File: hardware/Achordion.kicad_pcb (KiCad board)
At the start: 2 copper layers, 44.5 x 109.4 mm, 100 parts, among them J1 Power, J10 Jack, J11 Jack, J4 Jack, J5 Jack, J6 Jack, J7 Jack, J8 Jack, J9 Jack, SW2 Button, U4 LM4040C10, U6 TL072, U7 MCP6002, U8 MCP6002, U9 MCP6002

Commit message: Release version 0.10.0
Signed-off-by: Petr Horacek <hrck@protonmail.com>
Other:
- board text added: "board v0.10.0"
- board text removed: "board v0.9.0"

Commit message: Release version 0.11.0
Signed-off-by: Petr Horacek <hrck@protonmail.com>
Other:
- board text added: "board v0.11.0"
- board text removed: "board v0.10.0"
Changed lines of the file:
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@@
     (title Achordion)
     (date 2021-04-25)
-    (rev v0.10.0)
+    (rev v0.11.0)
     (company "Petr Horáček")
     (comment 1 hrck@protonmail.com)
@@
   (gr_circle (center 162.726001 144.48) (end 164.237002 144.48) (layer Edge.Cuts) (width 0.1))
   (gr_circle (center 139.236001 129.55) (end 140.747002 129.55) (layer Edge.Cuts) (width 0.1))
-  (gr_text "board v0.10.0" (at 156.325 42.775) (layer F.SilkS)
+  (gr_text "board v0.11.0" (at 156.325 42.775) (layer F.SilkS)
     (effects (font (size 1 1) (thickness 0.15)) (justify left))
   )

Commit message: Release version 0.12.0
Signed-off-by: Petr Horacek <hrck@protonmail.com>
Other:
- board text added: "board v0.12.0"
- board text removed: "board v0.11.0"
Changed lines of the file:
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@@
     (title Achordion)
     (date 2021-04-25)
-    (rev v0.11.0)
+    (rev v0.12.0)
     (company "Petr Horáček")
     (comment 1 hrck@protonmail.com)
@@
   (gr_circle (center 162.726001 144.48) (end 164.237002 144.48) (layer Edge.Cuts) (width 0.1))
   (gr_circle (center 139.236001 129.55) (end 140.747002 129.55) (layer Edge.Cuts) (width 0.1))
-  (gr_text "board v0.11.0" (at 156.325 42.775) (layer F.SilkS)
+  (gr_text "board v0.12.0" (at 156.325 42.775) (layer F.SilkS)
     (effects (font (size 1 1) (thickness 0.15)) (justify left))
   )

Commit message: Release version 0.13.0
Signed-off-by: Petr Horacek <hrck@protonmail.com>
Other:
- board text added: "board v0.13.0"
- board text removed: "board v0.12.0"
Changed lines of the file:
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@@
     (title Achordion)
     (date 2021-04-25)
-    (rev v0.12.0)
+    (rev v0.13.0)
     (company "Petr Horáček")
     (comment 1 hrck@protonmail.com)
@@
   (gr_circle (center 162.726001 144.48) (end 164.237002 144.48) (layer Edge.Cuts) (width 0.1))
   (gr_circle (center 139.236001 129.55) (end 140.747002 129.55) (layer Edge.Cuts) (width 0.1))
-  (gr_text "board v0.12.0" (at 156.325 42.775) (layer F.SilkS)
+  (gr_text "board v0.13.0" (at 156.325 42.775) (layer F.SilkS)
     (effects (font (size 1 1) (thickness 0.15)) (justify left))
   )

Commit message: Release version 0.14.0
Signed-off-by: Petr Horacek <hrck@protonmail.com>
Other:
- board text added: "board v0.14.0"
- board text removed: "board v0.13.0"
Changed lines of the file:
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@@
     (title Achordion)
     (date 2021-04-25)
-    (rev v0.13.0)
+    (rev v0.14.0)
     (company "Petr Horáček")
     (comment 1 hrck@protonmail.com)
@@
   (gr_circle (center 162.726001 144.48) (end 164.237002 144.48) (layer Edge.Cuts) (width 0.1))
   (gr_circle (center 139.236001 129.55) (end 140.747002 129.55) (layer Edge.Cuts) (width 0.1))
-  (gr_text "board v0.13.0" (at 156.325 42.775) (layer F.SilkS)
+  (gr_text "board v0.14.0" (at 156.325 42.775) (layer F.SilkS)
     (effects (font (size 1 1) (thickness 0.15)) (justify left))
   )

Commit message: Release version 0.15.0
Signed-off-by: Petr Horacek <hrck@protonmail.com>
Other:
- board text added: "board v0.15.0"
- board text removed: "board v0.14.0"
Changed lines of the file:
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@@
     (title Achordion)
     (date 2021-04-25)
-    (rev v0.14.0)
+    (rev v0.15.0)
     (company "Petr Horáček")
     (comment 1 hrck@protonmail.com)
@@
   (gr_circle (center 162.726001 144.48) (end 164.237002 144.48) (layer Edge.Cuts) (width 0.1))
   (gr_circle (center 139.236001 129.55) (end 140.747002 129.55) (layer Edge.Cuts) (width 0.1))
-  (gr_text "board v0.14.0" (at 156.325 42.775) (layer F.SilkS)
+  (gr_text "board v0.15.0" (at 156.325 42.775) (layer F.SilkS)
     (effects (font (size 1 1) (thickness 0.15)) (justify left))
   )

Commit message: Release version 0.16.0
Signed-off-by: Petr Horacek <hrck@protonmail.com>
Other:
- board text added: "board v0.16.0"
- board text removed: "board v0.15.0"
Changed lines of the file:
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@@
     (title Achordion)
     (date 2021-04-25)
-    (rev v0.15.0)
+    (rev v0.16.0)
     (company "Petr Horáček")
     (comment 1 hrck@protonmail.com)
@@
   (gr_circle (center 162.726001 144.48) (end 164.237002 144.48) (layer Edge.Cuts) (width 0.1))
   (gr_circle (center 139.236001 129.55) (end 140.747002 129.55) (layer Edge.Cuts) (width 0.1))
-  (gr_text "board v0.15.0" (at 156.325 42.775) (layer F.SilkS)
+  (gr_text "board v0.16.0" (at 156.325 42.775) (layer F.SilkS)
     (effects (font (size 1 1) (thickness 0.15)) (justify left))
   )

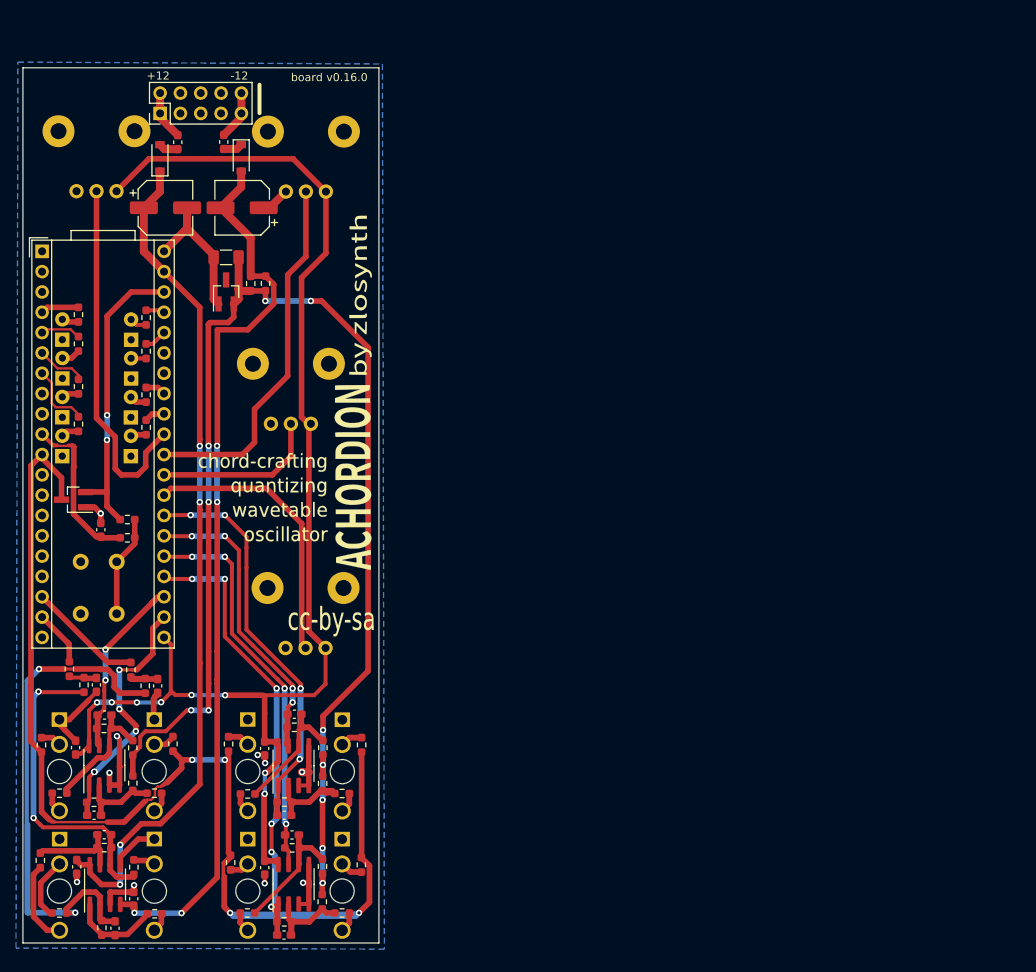
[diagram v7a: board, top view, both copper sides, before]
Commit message: Convert PCB to two stacked layers
This completely reworked layout should be much easier to solder and also
follows new front panel layout.

Signed-off-by: Petr Horacek <hrck@protonmail.com>
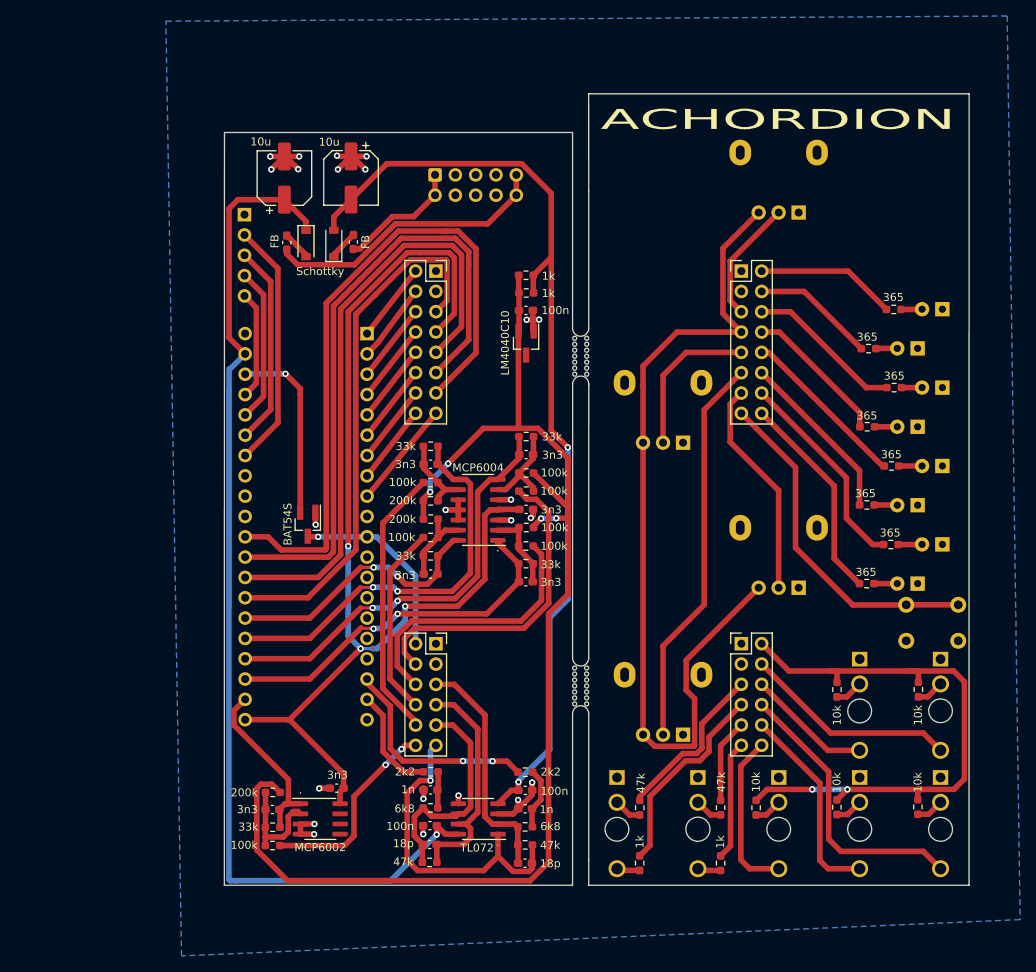
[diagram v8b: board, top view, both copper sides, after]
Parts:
- removed C39: 100n, Capacitor_SMD:C_0603_1608Metric_Pad1.08x0.95mm_HandSolder
- removed C45, C47: 3n3, Capacitor_SMD:C_0603_1608Metric_Pad1.08x0.95mm_HandSolder
- removed G***: LOGO, Graphics:Graphics_Back
- removed G***: LOGO, Graphics:Graphics_Front
- removed R15, R16, R49: 10k, Resistor_SMD:R_0603_1608Metric_Pad0.98x0.95mm_HandSolder
- removed R32: 200k, Resistor_SMD:R_0603_1608Metric_Pad0.98x0.95mm_HandSolder
- removed R33: 100k, Resistor_SMD:R_0603_1608Metric_Pad0.98x0.95mm_HandSolder
- removed R34: 33k, Resistor_SMD:R_0603_1608Metric_Pad0.98x0.95mm_HandSolder
- removed U7, U8: MCP6002, Package_SO:SOIC-8_3.9x4.9mm_P1.27mm
- added J12: Debug, Connector_PinHeader_2.54mm:PinHeader_1x05_P2.54mm_Vertical, B.Cu at (150.5, 59.9)
- added J13: A IFACE, Connector_PinHeader_2.54mm:PinHeader_2x08_P2.54mm_Vertical, F.Cu at (212.6, 67.0)
- added J2: B IFACE, Connector_PinSocket_2.54mm:PinSocket_2x08_P2.54mm_Vertical, F.Cu at (174.4, 67.0)
- added J3: B I/O, Connector_PinSocket_2.54mm:PinSocket_2x06_P2.54mm_Vertical, F.Cu at (174.4, 113.6)
- added U1: MCP6004, Package_SO:SOIC-14_3.9x8.7mm_P1.27mm, F.Cu at (179.7, 96.8)
- added mouse-bite-2mm-slot: VAL**, Panelization:mouse-bite-2mm-slot, F.Cu at (192.6, 118.8)
- added mouse-bite-2mm-slot: VAL**, Panelization:mouse-bite-2mm-slot, F.Cu at (192.6, 77.6)
- A1: value DaisySeed_Rev4 -> Daisy Seed v4; footprint Socket_DaisySeed:DaisySeed -> Device_Audio_Electrosmith_Daisy_Seed:Device_Audio_Electrosmith_Daisy_Seed; moved to B.Cu
- C21: footprint Capacitor_SMD:C_1206_3216Metric_Pad1.33x1.80mm_HandSolder -> Capacitor_SMD:C_0603_1608Metric_Pad1.08x0.95mm_HandSolder
- D10, D3, D4, D5, D6, D7, D8, D9: value LED_Small -> LED
- FB1, FB2: value Ferrite_Bead_Small -> FB
- J1: footprint Connector_PinHeader_2.54mm:PinHeader_2x05_P2.54mm_Vertical -> Connector_IDC:IDC-Header_2x05_P2.54mm_Vertical; moved to B.Cu
- J11: value Jack -> A I/O; footprint Connector_Audio:Jack_3.5mm_QingPu_WQP-PJ398SM_Vertical_CircularHoles -> Connector_PinHeader_2.54mm:PinHeader_2x06_P2.54mm_Vertical; moved to F.Cu
- RV1, RV2, RV3, RV4: footprint Potentiometer_THT:Potentiometer_Alps_RK09L_Single_Vertical -> Potentiometer_THT:Potentiometer_Alpha_RD901F-40-00D_Single_Vertical
- moved D10 111.5 mm to (237.8, 71.8), turned to 180 degrees
- moved D8 110.0 mm to (237.8, 81.5), turned to 180 degrees
- moved D7 107.5 mm to (234.7, 86.5), turned to 180 degrees
- moved D9 107.3 mm to (234.7, 76.7), turned to 180 degrees
- moved SW2 105.2 mm to (239.7, 108.7), turned to 180 degrees
- moved D4 103.5 mm to (237.8, 101.2), turned to 180 degrees
- moved D3 102.9 mm to (234.7, 106.0), turned to 180 degrees
- moved R42 102.9 mm to (231.7, 71.8), turned to 0 degrees
- moved R40 102.1 mm to (231.7, 81.5), turned to 0 degrees
- moved D6 101.4 mm to (237.8, 91.3), turned to 180 degrees
- moved R39 99.6 mm to (228.4, 86.5), turned to 0 degrees
- moved D5 98.9 mm to (234.7, 96.2), turned to 180 degrees
- moved R41 98.9 mm to (228.5, 76.7), turned to 0 degrees
- moved R36 96.2 mm to (231.3, 101.2), turned to 0 degrees
- moved R35 96.0 mm to (228.3, 106.0), turned to 0 degrees
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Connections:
- A1 pad 1: Net-(A1-Pad1) -> B_LED8
- A1 pad 10: BUTTON -> Net-(A1-Pad10)
- A1 pad 11: PROBE -> B_PROBE
- A1 pad 2: Net-(A1-Pad2) -> B_LED7
- A1 pad 22: CV3 -> CV5
- A1 pad 23: CV4 -> CV2
- A1 pad 24: CV5 -> CV1
- A1 pad 25: CV6 -> CV4
- A1 pad 26: CV2 -> CV3
- A1 pad 27: CV1 -> B_POT1
- A1 pad 28: POT4 -> B_POT2
- A1 pad 29: POT3 -> B_POT4
- A1 pad 3: Net-(A1-Pad3) -> B_LED6
- A1 pad 30: POT1 -> B_POT3
- A1 pad 31: POT2 -> Net-(A1-Pad31)
- A1 pad 32: LED4 -> Net-(A1-Pad32)
- A1 pad 33: LED3 -> Net-(A1-Pad33)
- A1 pad 34: Net-(A1-Pad34) -> GPIO1
- A1 pad 35: Net-(A1-Pad35) -> GPIO2
- A1 pad 36: LED2 -> GPIO3
- A1 pad 37: LED1 -> GPIO4
- A1 pad 4: LED5 -> B_LED5
- A1 pad 5: LED6 -> B_LED4
- A1 pad 6: LED7 -> B_LED3
- A1 pad 7: LED8 -> B_LED2
- A1 pad 8: Net-(A1-Pad8) -> B_LED1
- A1 pad 9: Net-(A1-Pad9) -> B_BUTTON
- C36 pad 1: Net-(C36-Pad1) -> B_OUT1_MAIN
- C36 pad 2: Net-(C36-Pad2) -> B_OUT2_FALL
- C38 pad 1: Net-(C38-Pad1) -> B_OUT2_MAIN
- C38 pad 2: Net-(C38-Pad2) -> B_OUT1_FALL
- C40 pad 1: CV1 -> CV2
- C41 pad 1: CV2 -> CV1
- C42 pad 1: CV5 -> CV4
- C43 pad 1: CV6 -> CV3
- C44 pad 1: CV3 -> CV5
- D11 pad 3: PROBE -> B_PROBE
- J1 pad 1: Net-(FB1-Pad2) -> Net-(FB2-Pad2)
- J1 pad 10: Net-(FB2-Pad2) -> Net-(FB1-Pad2)
- J1 pad 2: Net-(FB1-Pad2) -> Net-(FB2-Pad2)
- J1 pad 9: Net-(FB2-Pad2) -> Net-(FB1-Pad2)
- J10 pad T: Net-(J10-PadT) -> A_CV5_IN
- J6 pad T: Net-(J6-PadT) -> A_CV1_IN
- J7 pad T: Net-(J7-PadT) -> A_CV2_IN
- J8 pad T: Net-(J8-PadT) -> A_CV3_IN
- J9 pad T: Net-(J9-PadT) -> A_CV4_IN
- R10 pad 1: Net-(C36-Pad1) -> A_OUT1_MAIN
- R12 pad 2: Net-(C38-Pad2) -> B_OUT1_FALL
- R13 pad 1: Net-(C38-Pad2) -> B_OUT1_FALL
- R13 pad 2: Net-(C38-Pad1) -> B_OUT2_MAIN
- R14 pad 1: Net-(C38-Pad1) -> A_OUT2_MAIN
- R18 pad 1: Net-(J6-PadT) -> B_CV2_IN
- R19 pad 2: CV1 -> CV2
- R21 pad 1: Net-(J7-PadT) -> B_CV1_IN
- R22 pad 2: CV2 -> CV1
- R25 pad 1: Net-(J8-PadT) -> B_CV4_IN
- R26 pad 2: CV5 -> CV4
- R28 pad 1: Net-(J9-PadT) -> B_CV3_IN
- R29 pad 2: CV6 -> CV3
- R30 pad 1: Net-(J10-PadT) -> B_CV5_IN
- R31 pad 2: CV3 -> CV5
- R35 pad 1: LED1 -> A_LED1
- R36 pad 1: LED2 -> A_LED2
- R37 pad 1: LED3 -> A_LED3
- R38 pad 1: LED4 -> A_LED4
- R39 pad 1: LED5 -> A_LED5
- R40 pad 1: LED6 -> A_LED6
- R41 pad 1: LED7 -> A_LED7
- R42 pad 1: LED8 -> A_LED8
- R43 pad 1: PROBE -> A_PROBE
- R45 pad 1: PROBE -> A_PROBE
- R46 pad 1: PROBE -> A_PROBE
- R47 pad 1: PROBE -> A_PROBE
- R48 pad 1: PROBE -> A_PROBE
- R50 pad 2: Net-(C36-Pad2) -> A_OUT2_FALL
- R51 pad 2: Net-(C38-Pad2) -> A_OUT1_FALL
- R8 pad 2: Net-(C36-Pad2) -> B_OUT2_FALL
- R9 pad 1: Net-(C36-Pad2) -> B_OUT2_FALL
- R9 pad 2: Net-(C36-Pad1) -> B_OUT1_MAIN
- RV1 pad 2: POT1 -> A_POT1
- RV2 pad 2: POT2 -> A_POT2
- RV3 pad 2: POT3 -> A_POT3
- RV4 pad 2: POT4 -> A_POT4
- SW2 pad 1: Net-(R15-Pad2) -> A_BUTTON
- U6 pad 1: Net-(C36-Pad1) -> B_OUT1_MAIN
- U6 pad 2: Net-(C36-Pad2) -> B_OUT2_FALL
- U6 pad 6: Net-(C38-Pad2) -> B_OUT1_FALL
- U6 pad 7: Net-(C38-Pad1) -> B_OUT2_MAIN
- U9 pad 1: CV3 -> CV5
- U9 pad 5: GND -> Net-(U9-Pad5)
- U9 pad 7: CV4 -> Net-(U9-Pad7)
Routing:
- net PROBE: track 278.4 -> 0.00 mm, vias 4 -> 0
- net Net-(C36-Pad2): track 90.9 -> 0.00 mm, vias 2 -> 0
- net B_POT3: track 0.00 -> 85.0 mm
- net B_POT4: track 0.00 -> 80.0 mm
- net B_POT2: track 0.00 -> 76.2 mm
- net A_PROBE: track 0.00 -> 73.8 mm, vias 0 -> 2
- net B_POT1: track 0.00 -> 67.0 mm
- net CV6: track 49.5 -> 0.00 mm, vias 4 -> 0
- net A_POT4: track 0.00 -> 49.3 mm
- net +3.3VA: track 193.8 -> 242.8 mm, vias 8 -> 3
- net POT2: track 46.3 -> 0.00 mm
- net POT1: track 46.0 -> 0.00 mm
- net GND: track 93.5 -> 48.7 mm, vias 10 -> 23
- net A_BUTTON: track 0.00 -> 42.9 mm
- net CV5: track 63.3 -> 21.7 mm, vias 6 -> 0
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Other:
- board size 44.5 x 109.4 mm -> 93.1 x 98.9 mm
- board text added: "."
- board text added: "1"
- board text added: "2"
- board text added: "3"
- board text added: "4"
- board text added: "ACHORDION"
- board text added: "board v1.0.0-rc.1"
- board text added: "by ZLOSYNTH"
- board text removed: "+12"
- board text removed: "-12"
- board text removed: "3V3"
- board text removed: "3VA3"
- board text removed: "B"
- board text removed: "BUTTON"
- board text removed: "C1"
- board text removed: "C2"
- board text removed: "C3"
- board text removed: "C4"
- board text removed: "C5"
- board text removed: "C6"
- board text removed: "CV1"
- board text removed: "CV2"
- board text removed: "CV3"
- board text removed: "CV4"
- board text removed: "CV5"
- board text removed: "CV6"
- board text removed: "D1"
- board text removed: "D2"
- board text removed: "DAC1"
- board text removed: "DAC2"
- board text removed: "Daisy Seed"
- board text removed: "L1"
- board text removed: "L2"
- board text removed: "L3"
- board text removed: "L4"
- board text removed: "L5"
- board text removed: "L6"
- board text removed: "L7"
- board text removed: "L8"
- board text removed: "LED1"
- board text removed: "LED2"
- board text removed: "LED3"
- board text removed: "LED4"
- board text removed: "LED5"
- board text removed: "LED6"
- board text removed: "LED7"
- board text removed: "LED8"
- board text removed: "P"
- board text removed: "P1"
- board text removed: "P2"
- board text removed: "P3"
- board text removed: "P4"
- board text removed: "POT1"
- board text removed: "POT2"
- board text removed: "POT3"
- board text removed: "POT4"
- board text removed: "VCC"
- board text removed: "board v0.16.0"
